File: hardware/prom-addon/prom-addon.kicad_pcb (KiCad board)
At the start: 2 copper layers, 10 parts, among them J1 Conn_02x10_Odd_Even, J2 Conn_02x10_Odd_Even, U1 74HC595, U2 74HC595, U3 27C512

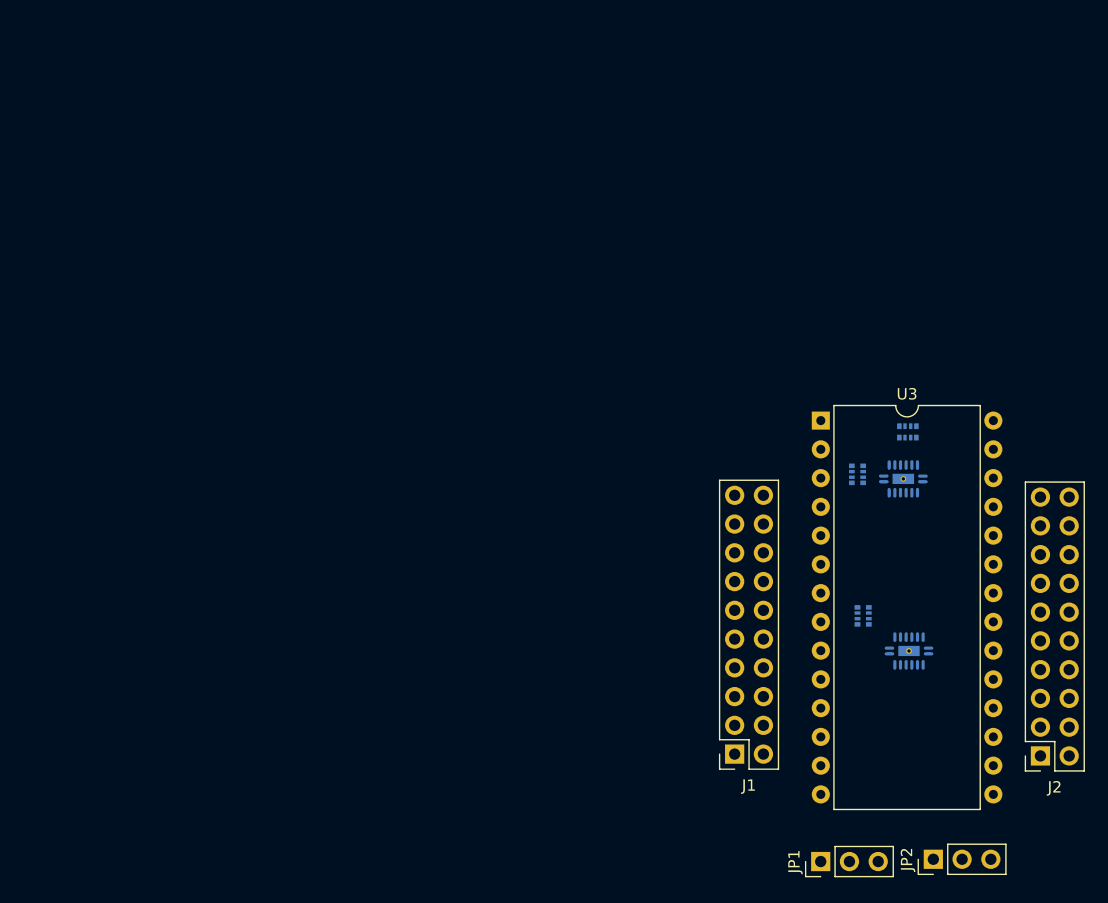
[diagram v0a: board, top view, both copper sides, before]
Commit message: prom: Routed the first version of the board.
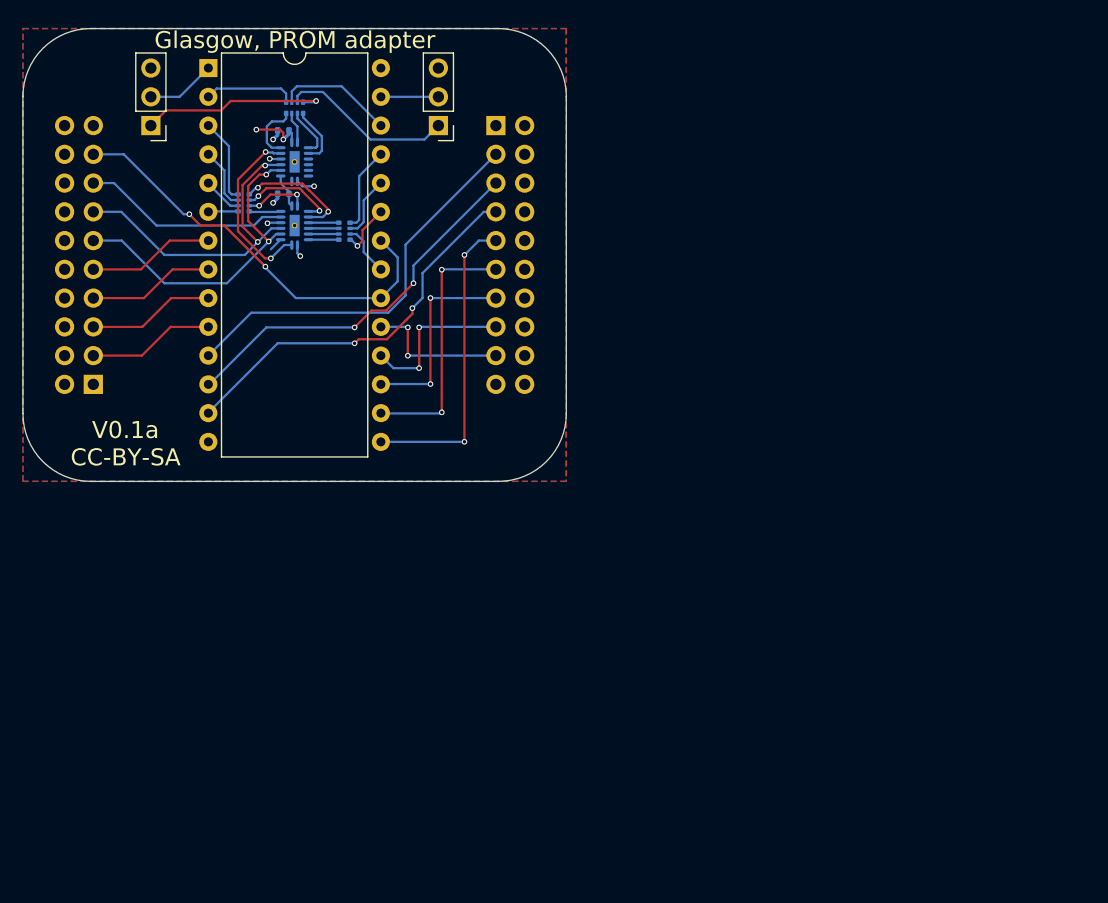
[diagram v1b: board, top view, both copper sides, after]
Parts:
- added C1: 100n, pkl_dipol:C_0402, B.Cu at (54.9, 41.1)
- added C2: 100n, pkl_dipol:C_0402, B.Cu at (54.9, 46.7)
- J1, J2: moved to B.Cu
- moved JP2 94.8 mm to (43.2, 40.6), turned to 180 degrees
- moved J2 73.6 mm to (73.7, 40.6)
- moved JP1 73.3 mm to (68.6, 40.6), turned to 180 degrees
- moved U2 69.4 mm to (55.9, 43.8), turned to 270 degrees
- moved RN3 67.4 mm to (55.9, 39.1), turned to 270 degrees
- moved J1 65.4 mm to (38.1, 63.5), turned to 0 degrees
- moved U3 62.4 mm to (48.3, 35.6)
- moved RN1 59.3 mm to (51.4, 47.5)
- moved U1 58.2 mm to (55.9, 49.5), turned to 270 degrees
- moved RN2 52.8 mm to (60.3, 50.0), turned to 180 degrees
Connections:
- J1 pad 11: /A_LATCH -> /A_CLK
- J1 pad 13: /A_CLK -> /A_LATCH
- RN1 pad 1: Net-(RN1-Pad1) -> /A4
- RN1 pad 2: Net-(RN1-Pad2) -> /A5
- RN1 pad 3: Net-(RN1-Pad3) -> /A6
- RN1 pad 4: Net-(RN1-Pad4) -> /A7
- RN1 pad 5: /A7 -> Net-(RN1-Pad5)
- RN1 pad 6: /A6 -> Net-(RN1-Pad6)
- RN1 pad 7: /A5 -> Net-(RN1-Pad7)
- RN1 pad 8: /A4 -> Net-(RN1-Pad8)
- RN2 pad 1: Net-(RN2-Pad1) -> /A8
- RN2 pad 2: Net-(RN2-Pad2) -> /A9
- RN2 pad 3: Net-(RN2-Pad3) -> /A10
- RN2 pad 4: Net-(RN2-Pad4) -> /A11
- RN2 pad 5: /A11 -> Net-(RN2-Pad5)
- RN2 pad 6: /A10 -> Net-(RN2-Pad6)
- RN2 pad 7: /A9 -> Net-(RN2-Pad7)
- RN2 pad 8: /A8 -> Net-(RN2-Pad8)
- RN3 pad 1: Net-(RN3-Pad1) -> /A12
- RN3 pad 2: Net-(RN3-Pad2) -> /A13
- RN3 pad 3: Net-(RN3-Pad3) -> /A14
- RN3 pad 4: Net-(RN3-Pad4) -> /A15
- RN3 pad 5: /A15 -> Net-(RN3-Pad5)
- RN3 pad 6: /A14 -> Net-(RN3-Pad6)
- RN3 pad 7: /A13 -> Net-(RN3-Pad7)
- RN3 pad 8: /A12 -> Net-(RN3-Pad8)
- U1 pad 1: Net-(RN1-Pad2) -> Net-(RN1-Pad7)
- U1 pad 15: Net-(RN1-Pad1) -> Net-(RN1-Pad8)
- U1 pad 2: Net-(RN1-Pad3) -> Net-(RN1-Pad6)
- U1 pad 3: Net-(RN1-Pad4) -> Net-(RN1-Pad5)
- U1 pad 4: Net-(RN2-Pad1) -> Net-(RN2-Pad8)
- U1 pad 5: Net-(RN2-Pad2) -> Net-(RN2-Pad7)
- U1 pad 6: Net-(RN2-Pad3) -> Net-(RN2-Pad6)
- U1 pad 7: Net-(RN2-Pad4) -> Net-(RN2-Pad5)
- U2 pad 1: Net-(RN3-Pad2) -> Net-(RN3-Pad7)
- U2 pad 15: Net-(RN3-Pad1) -> Net-(RN3-Pad8)
- U2 pad 2: Net-(RN3-Pad3) -> Net-(RN3-Pad6)
- U2 pad 3: Net-(RN3-Pad4) -> Net-(RN3-Pad5)
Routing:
- net /~OE: track 0.00 -> 37.0 mm, vias 0 -> 2
- net /DQ0: track 0.00 -> 35.4 mm
- net /DQ2: track 0.00 -> 34.4 mm, vias 0 -> 2
- net /DQ1: track 0.00 -> 33.7 mm, vias 0 -> 2
- net /A_CLK: track 0.00 -> 29.0 mm, vias 0 -> 2
- net /A_LATCH: track 0.00 -> 28.8 mm, vias 0 -> 2
- net /DQ3: track 0.00 -> 27.2 mm, vias 0 -> 2
- net /DQ4: track 0.00 -> 23.2 mm, vias 0 -> 2
- net /A_SI: track 0.00 -> 18.4 mm
- net /DQ5: track 0.00 -> 17.8 mm, vias 0 -> 2
- net /A15: track 0.00 -> 16.7 mm, vias 0 -> 1
- net /A_SI´: track 0.00 -> 15.6 mm, vias 0 -> 2
- net /A14: track 0.00 -> 15.4 mm
- net /DQ6: track 0.00 -> 14.2 mm, vias 0 -> 2
- net /DQ7: track 0.00 -> 12.7 mm, vias 0 -> 2
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- added copper zone on F.Cu, net GND
- added copper zone on B.Cu, net VCC
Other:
- board outline added: 48 x 40 mm
- net class Default: trace_width 0.25 -> 0.2; via_dia 0.8 -> 0.5; via_drill 0.4 -> 0.3
- rule via_min_size: 0.4 -> 0.5
- board text added: "Glasgow, PROM adapter"
- board text added: "V0.1a CC-BY-SA"

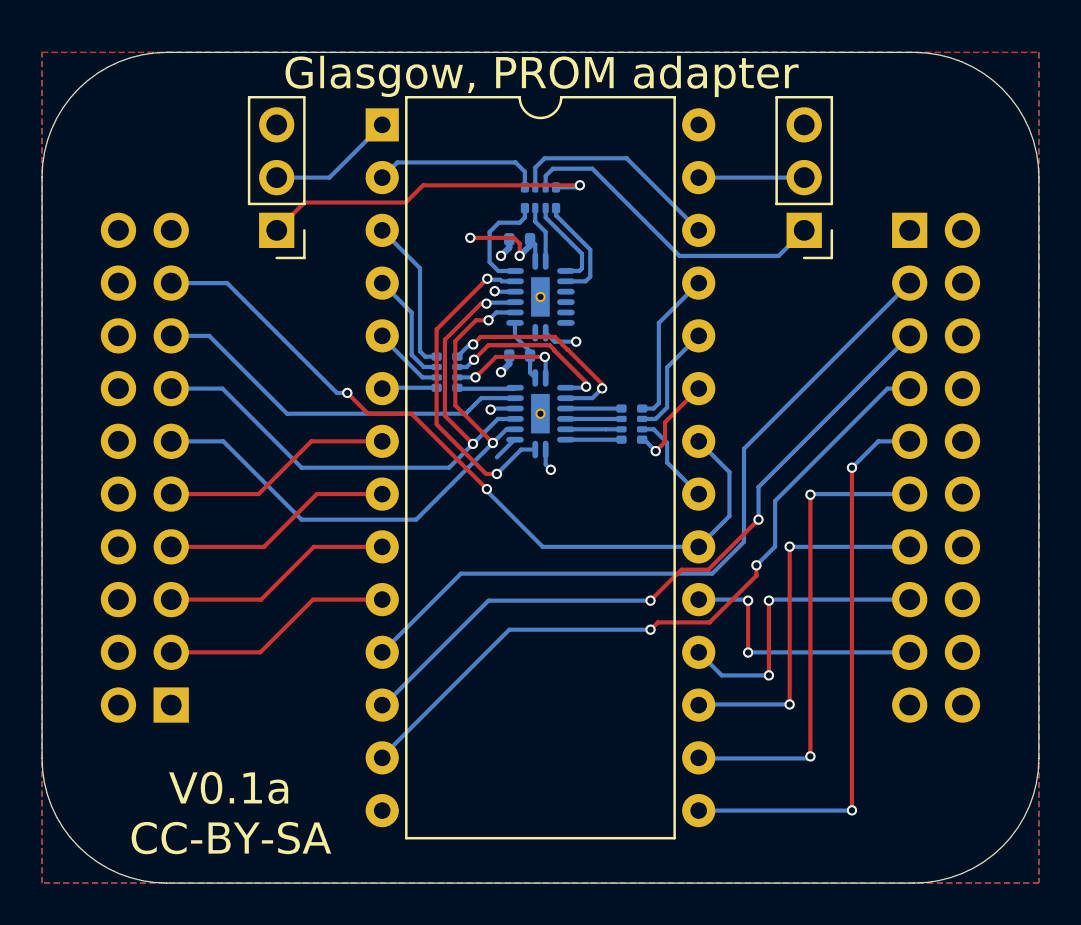
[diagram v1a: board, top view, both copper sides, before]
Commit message: Replaced supply fills with point to point routing.
Will look better in afterdark. ;)
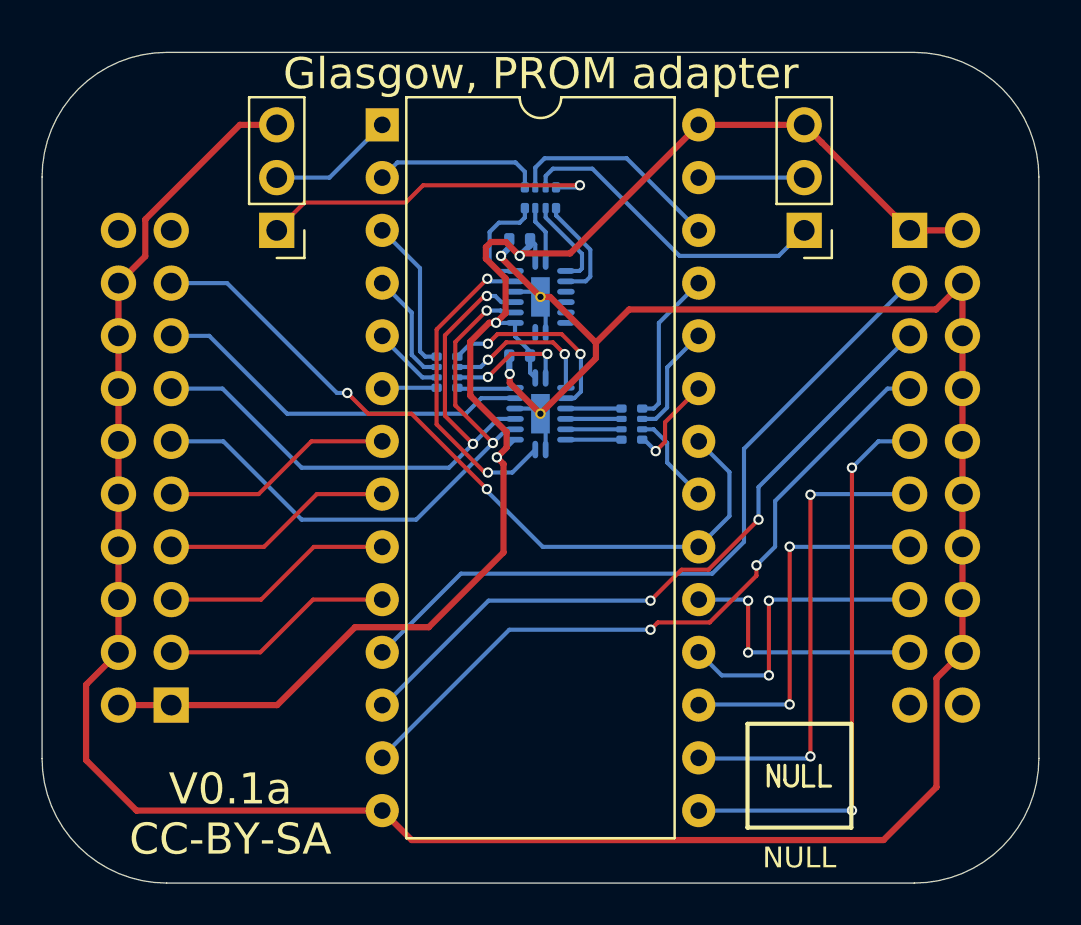
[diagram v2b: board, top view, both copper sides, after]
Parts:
- added REF**: null_Logo_SilkS_10mm, pkl_logos:null_Logo_SilkS_10mm, B.Cu at (55.9, 61.9)
- added REF**: null_Logo_SilkS_5mm, pkl_logos:null_Logo_SilkS_5mm, F.Cu at (68.3, 66.9)
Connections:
- U1 pad 17: (no net) -> GND
- U2 pad 17: (no net) -> GND
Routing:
- net GND: track 6.84 -> 143.3 mm, vias 6 -> 2
- net VCC: track 9.53 -> 74.0 mm, vias 2 -> 3
- net Net-(RN1-Pad6): track 8.60 -> 7.54 mm
- net Net-(RN1-Pad5): track 10.5 -> 9.48 mm
- removed copper zone on F.Cu, net GND
- removed copper zone on B.Cu, net VCC
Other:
- rule pad_to_mask_clearance: 0.05 -> 0
- board text added: "NULL"

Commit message: Silkscreen minor fixes.
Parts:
- moved REF** 2.05 mm to (55.9, 63.9), turned to 180 degrees

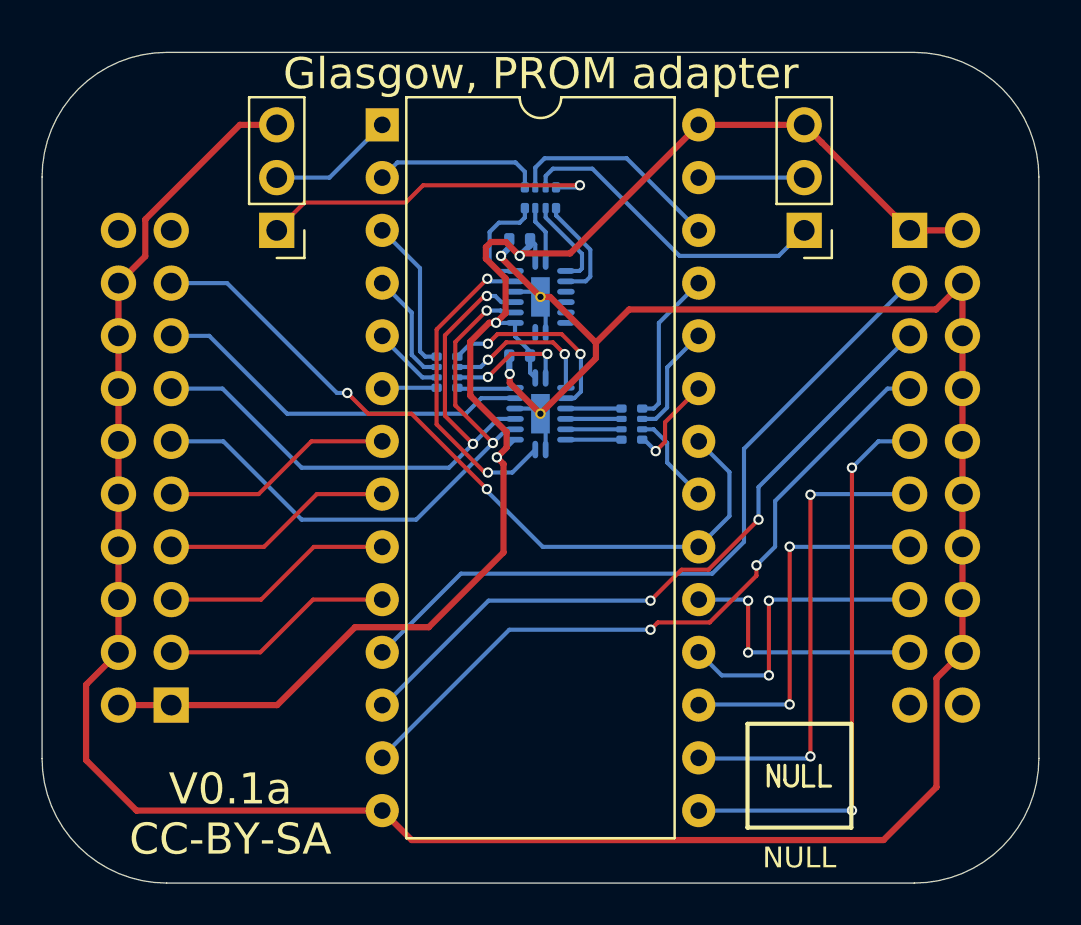
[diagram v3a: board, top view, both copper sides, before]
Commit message: prom: Added silkscreen legend. Bumped version.
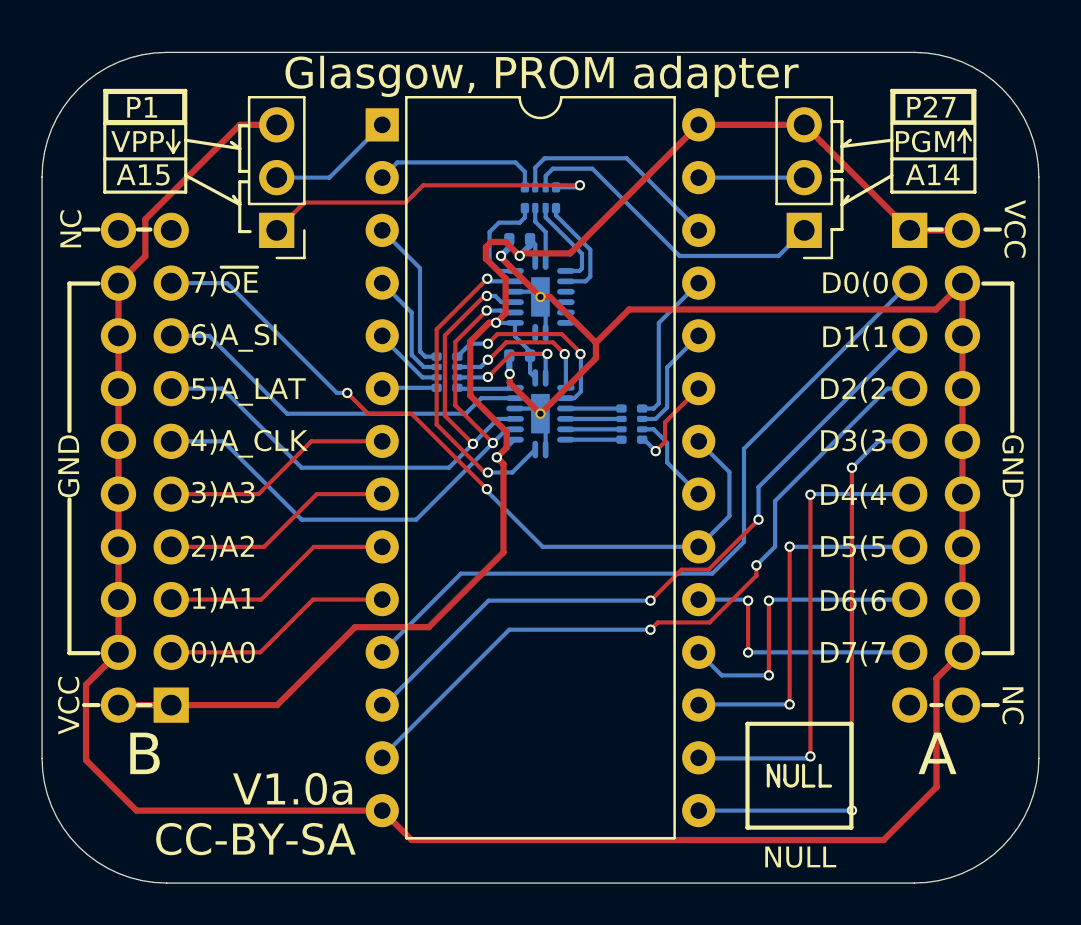
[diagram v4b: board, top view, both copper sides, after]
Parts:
- RN1, RN2, RN3: value 100R -> 33R
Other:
- board text added: "0)A0"
- board text added: "0)D0"
- board text added: "1)A1"
- board text added: "1)D1"
- board text added: "2)A2"
- board text added: "2)D2"
- board text added: "3)A3"
- board text added: "3)D3"
- board text added: "4)A_CLK"
- board text added: "4)D4"
- board text added: "5)A_LAT"
- board text added: "5)D5"
- board text added: "6)A_SI"
- board text added: "6)D6"
- board text added: "7)D7"
- board text added: "7)~OE"
- board text added: "A"
- board text added: "A0(0"
- board text added: "A1(1"
- board text added: "A14"
- board text added: "A15"
- board text added: "A2(2"
- board text added: "A3(3"
- board text added: "A_CLK(4"
- board text added: "A_LAT(5"
- board text added: "A_SI(6"
- board text added: "B"
- board text added: "D0(0"
- board text added: "D1(1"
- board text added: "D2(2"
- board text added: "D3(3"
- board text added: "D4(4"
- board text added: "D5(5"
- board text added: "D6(6"
- board text added: "D7(7"
- board text added: "GND"
- board text added: "NC"
- board text added: "P1"
- board text added: "P27"
- board text added: "PGM"
- board text added: "V1.0a CC-BY-SA"
- board text added: "VCC"
- board text added: "VPP"
- board text added: "~OE(7"
- board text removed: "V0.1a CC-BY-SA"
